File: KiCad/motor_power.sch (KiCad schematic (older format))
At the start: 63 parts, among them Q1 Q_PMOS_SGD, Q10 Q_NMOS_DGS, Q11 Q_PMOS_DGS, Q12 Q_PMOS_DGS, Q13 Q_PMOS_SGD, Q14 Q_PMOS_SGD, Q15 Q_NMOS_DGS, Q16 Q_NMOS_DGS, Q17 Q_PMOS_DGS, Q18 Q_PMOS_DGS, Q19 Q_PMOS_SGD, Q2 Q_PMOS_SGD, Q20 Q_PMOS_SGD, Q21 Q_NMOS_DGS, Q22 Q_NMOS_DGS, Q23 Q_PMOS_DGS, Q24 Q_PMOS_DGS, Q3 Q_NMOS_DGS, Q4 Q_NMOS_DGS, Q5 Q_PMOS_DGS, Q6 Q_PMOS_DGS, Q7 Q_PMOS_SGD, Q8 Q_PMOS_SGD, Q9 Q_NMOS_DGS, U3 INA219

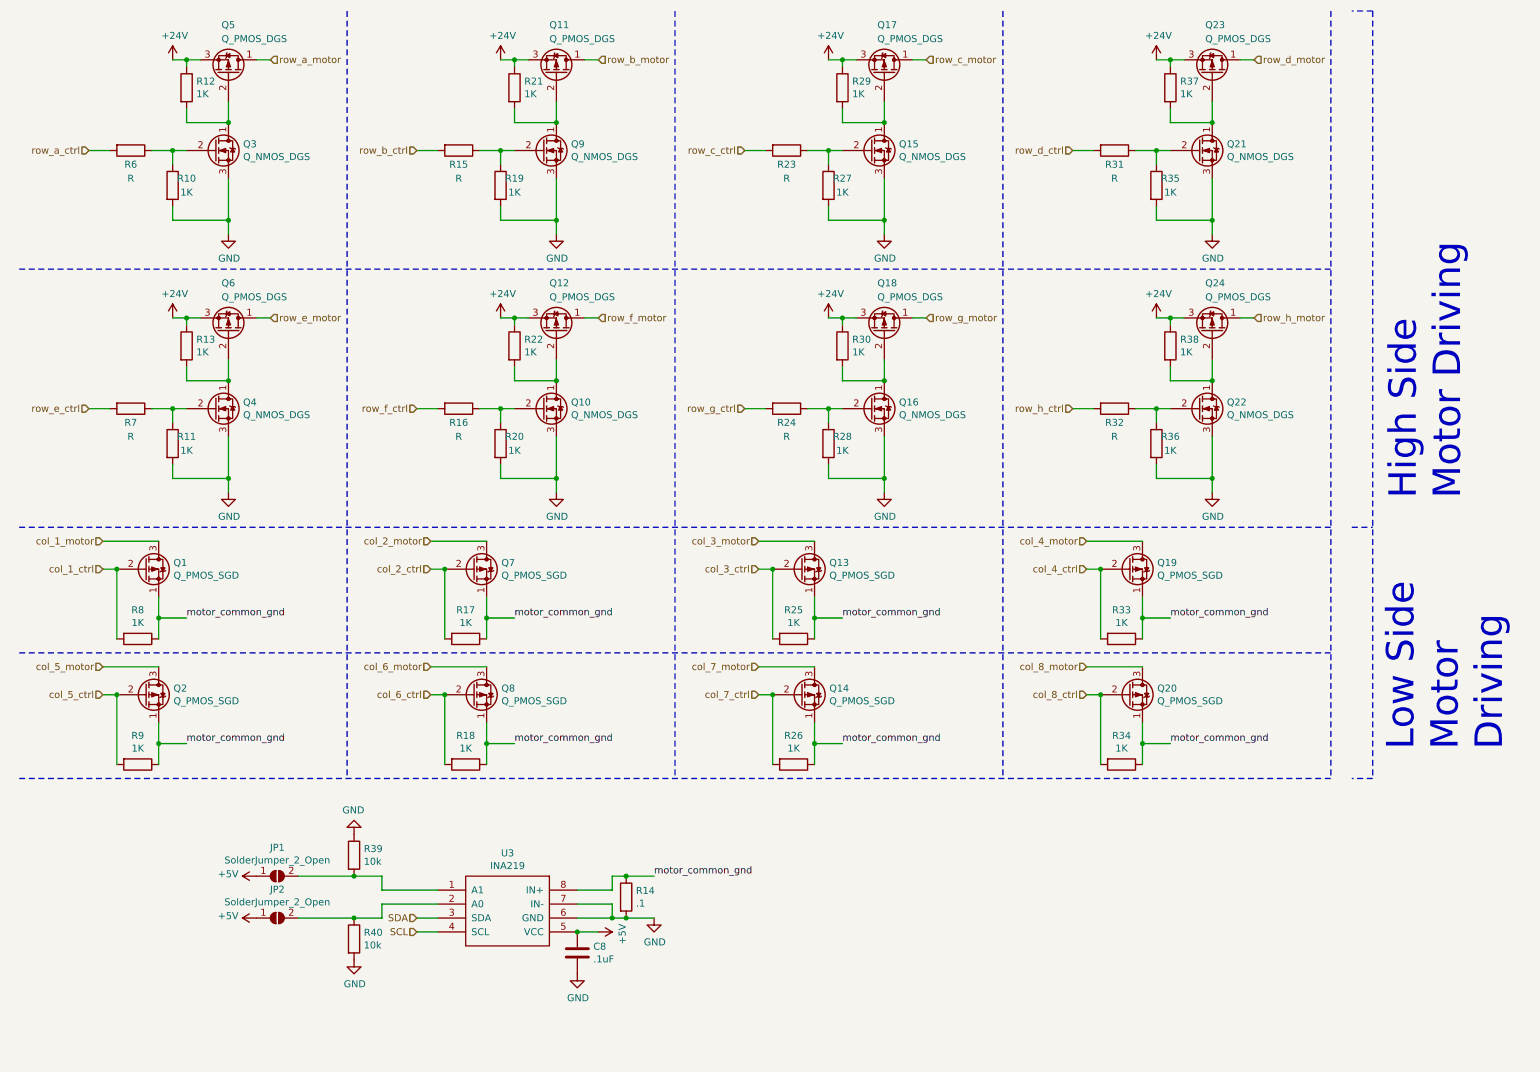
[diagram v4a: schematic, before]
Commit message: Large number of changes, some cosmetic, most functional. Added analog current sense circuit, added switching power supply (24V->5V), added switch connector for sensing when door is open, added LCD12864 connectors, added RFID125kHz connectors, modified multi-drop bus connection, updated bootloader hardware to match Arduino MEGA R3 circuit, plus other small changes.
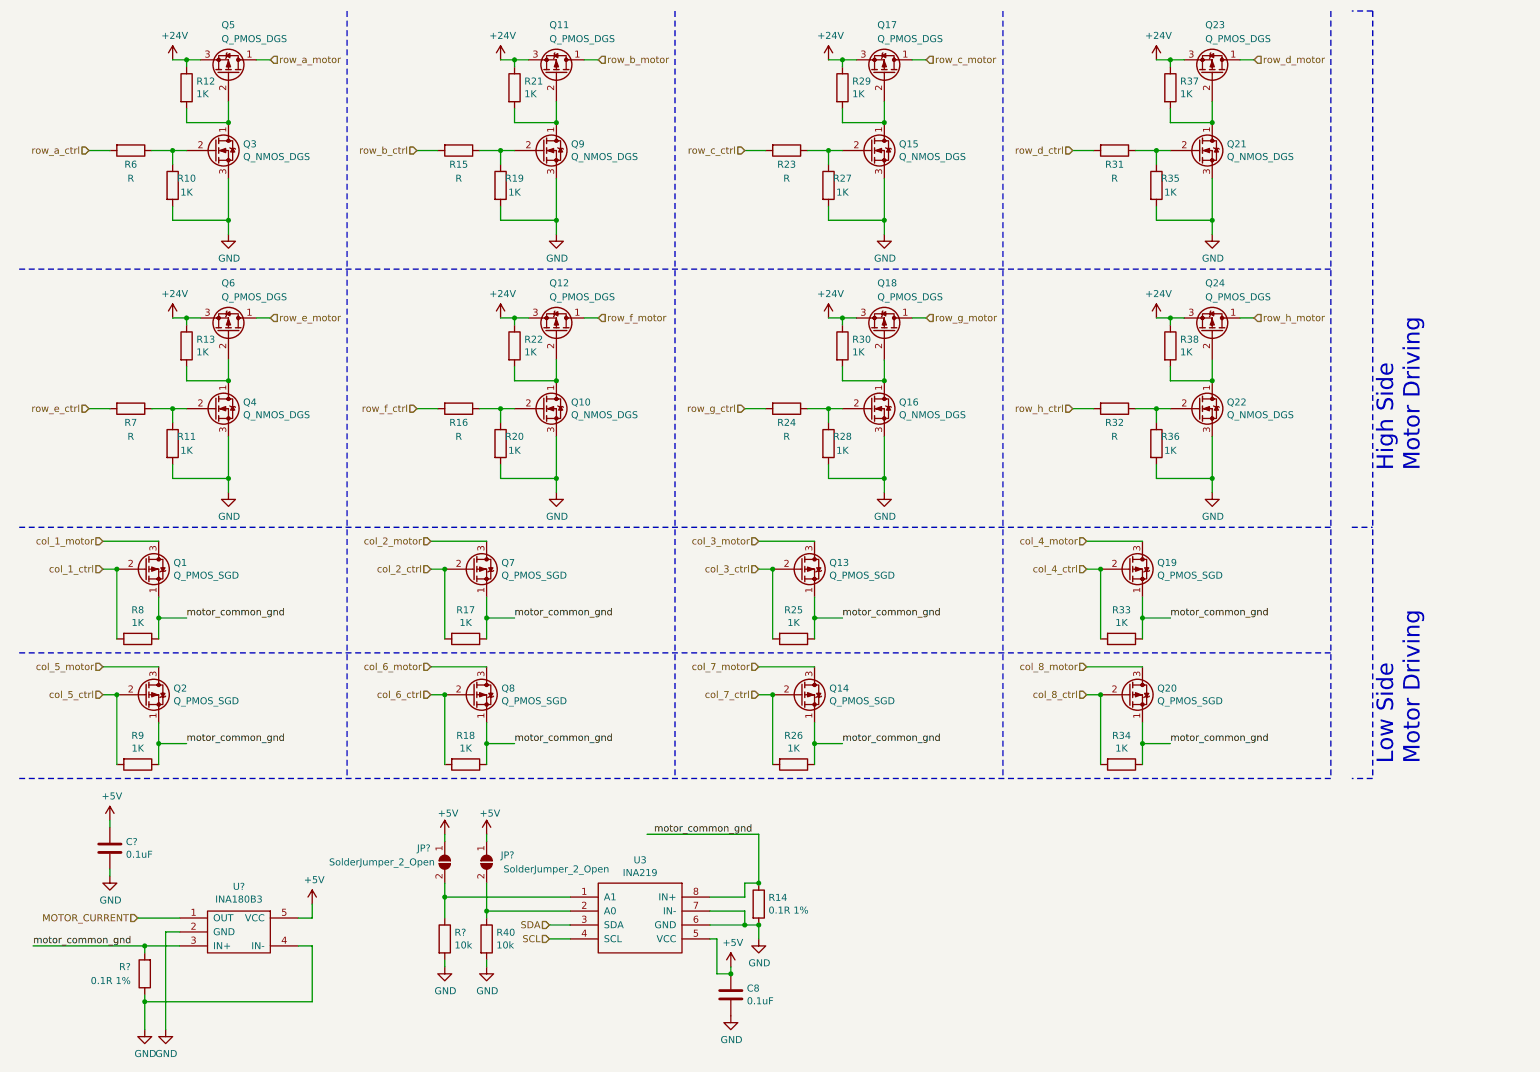
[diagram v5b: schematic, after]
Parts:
- removed JP1, JP2: SolderJumper_2_Open, symbol Jumper:SolderJumper_2_Open
- removed R39: 10k, symbol Device:R
- added C?: 0.1uF, symbol Device:C
- added JP? (x2): SolderJumper_2_Open, symbol Jumper:SolderJumper_2_Open
- added R?: 0.1R 1%, symbol Device:R
- added R?: 10k, symbol Device:R
- added U?: INA180B3, symbol Snack_Machine:INA180B3
- C8: value .1uF -> 0.1uF
- R14: value .1 -> 0.1R 1%
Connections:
- net +5V: now also C?.1, JP?.1 (A), JP?.1 (A), U?.5 (VCC)
- net GND: now also C?.2, R?.1, R?.2, U?.2 (GND), U?.4 (IN-)
- net motor_common_gnd: now also R?.2, U?.3 (IN+)
- net at U3.1 (A1): now also JP?.2 (B), R?.1
- net at R40.1, U3.2 (A0): now also JP?.2 (B)
- new net MOTOR_CURRENT: U?.1 (OUT)
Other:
- note added: "Low Side\nMotor Driving"
- note removed: "Low Side\nMotor\nDriving"
- moved on the sheet: C8, R14, R40, U3

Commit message: Updating annotations for all schematics
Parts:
- gave numbers to parts that had none: 6
- renumbered C8 to C14, Q6 to Q10, Q12 to Q11, Q18 to Q12, Q24 to Q13, Q4 to Q14, Q10 to Q15, Q22 to Q17, Q1 to Q18, Q7 to Q19, Q5 to Q2, Q13 to Q20, Q19 to Q21, Q2 to Q22, Q8 to Q23, Q14 to Q24, Q20 to Q25, Q11 to Q3, Q17 to Q4, Q23 to Q5, Q3 to Q6, Q9 to Q7, Q15 to Q8, Q21 to Q9, R12 to R13, R21 to R14, R29 to R15, R37 to R16, R6 to R17, R15 to R18, R23 to R19, R31 to R20, R10 to R21, R19 to R22, R27 to R23, R35 to R24, R13 to R25, R22 to R26, R30 to R27, R38 to R28, R7 to R29, R16 to R30, R24 to R31, R11 to R33, R20 to R34, R28 to R35, R8 to R37, R17 to R38, R25 to R39, R33 to R40, R9 to R41, R18 to R42, R26 to R43, R34 to R44, R14 to R45, R40 to R47, U3 to U4

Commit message: Updating components and footprints
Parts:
- removed Q18, Q19, Q20, Q21, Q22, Q23, Q24, Q25: Q_PMOS_SGD, symbol Device:Q_PMOS_SGD
- added Q18, Q19, Q20, Q21, Q22, Q23, Q24, Q25: Q_NMOS_SGD, symbol Device:Q_NMOS_SGD
- C13, C14: footprint (none) -> Capacitor_SMD:C_0603_1608Metric_Pad1.05x0.95mm_HandSolder
- R13, R14, R15, R16, R17, R18, R19, R20, R21, R22, R23, R24, R25, R26, R27, R28, R29, R30, R31, R32, R33, R34, R35, R36, R37, R38, R39, R40, R41, R42, R43, R44, R46, R47, R48: footprint (none) -> Resistor_SMD:R_0603_1608Metric_Pad1.05x0.95mm_HandSolder
- R45: footprint (none) -> Resistor_SMD:R_0805_2012Metric

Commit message: changed all mosfets
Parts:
- removed Q11, Q12, Q13, Q2, Q3, Q4, Q5: Q_PMOS_DGS, symbol Device:Q_PMOS_DGS
- removed Q15, Q16, Q17, Q6, Q7, Q8, Q9: Q_NMOS_DGS, symbol Device:Q_NMOS_DGS
- removed Q19, Q20, Q21, Q22, Q23, Q24, Q25: Q_NMOS_SGD, symbol Device:Q_NMOS_SGD
- added Q? (x7): P-CH 30V 3.8A, symbol Device:Q_PMOS_GSD
- added Q? (x7): N-CH 50V 200mA, symbol Device:Q_NMOS_GSD
- added Q? (x7): Q_NMOS_SGD, symbol Device:Q_NMOS_GSD
- Q10: value Q_PMOS_DGS -> P-CH 30V 3.8A; symbol Device:Q_PMOS_DGS -> Device:Q_PMOS_GSD; Manufacturer (none) -> Diodes Incorporated; Part Number (none) -> DMP3099L-7
- Q14: value Q_NMOS_DGS -> N-CH 50V 200mA; symbol Device:Q_NMOS_DGS -> Device:Q_NMOS_GSD; Manufacturer (none) -> Rohm Semiconductor; Part Number (none) -> RUC002N05HZGT116
- Q18: symbol Device:Q_NMOS_SGD -> Device:Q_NMOS_GSD; Manufacturer (none) -> ON Semiconductor; Part Number (none) -> NTR4003NT1G
